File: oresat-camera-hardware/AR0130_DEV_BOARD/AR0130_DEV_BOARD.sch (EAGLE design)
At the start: 60 parts, among them J2 4-1734592-0, U10 SN74AVCB164245VR, U11 KC2520B27.0000C10E00, U12 TPS71818-33DRVT, U13 SN74AVCH8T245RHLR, U14 TPS71928-28DRVT, U15 TPS71928-28DRVT, U6 MCP9808T-E/MCDFN8_2X3MC-M, U7 MCP9808T-E/MCDFN8_2X3MC-M, U9 TCA9509DGKRDGK8-M

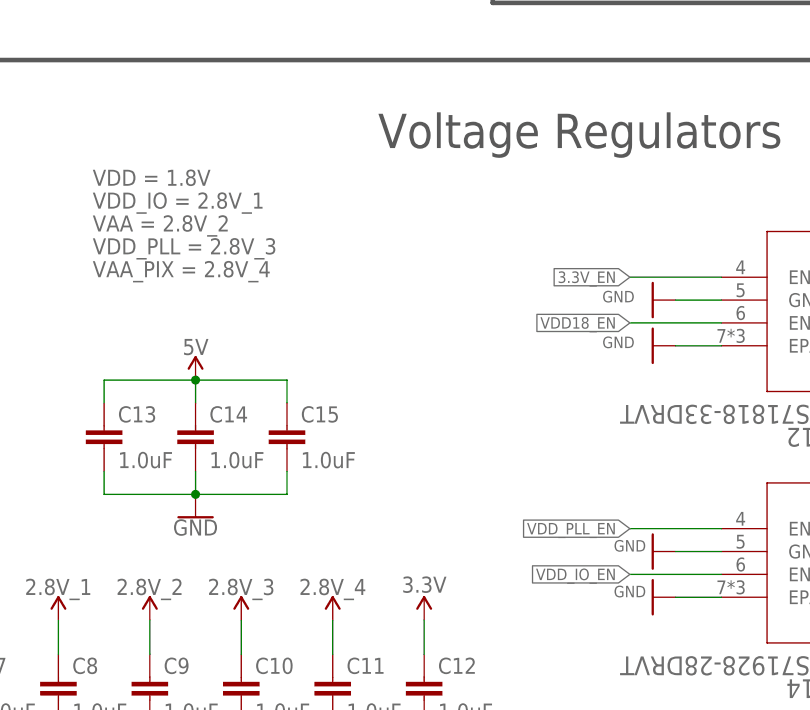
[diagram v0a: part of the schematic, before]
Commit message: added a LED
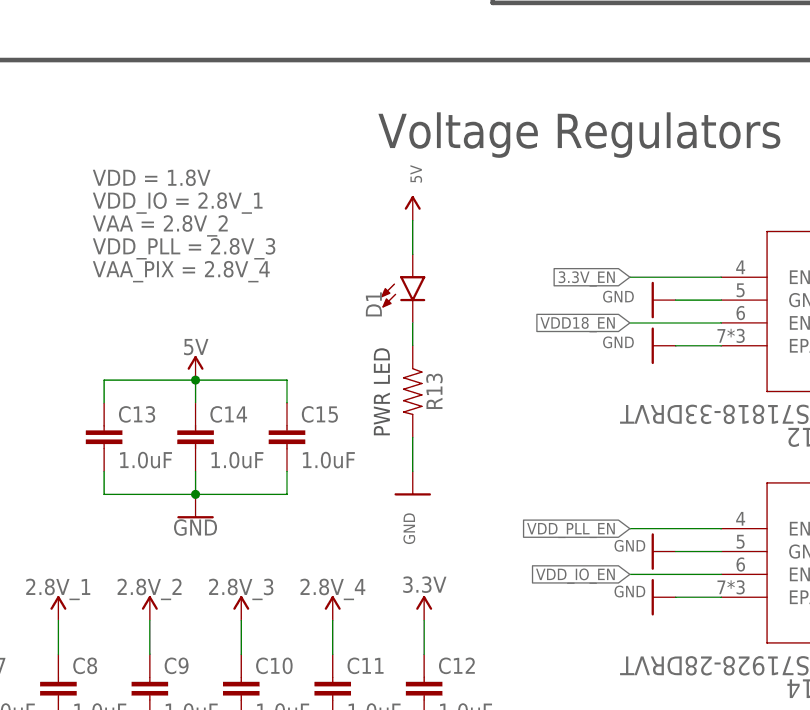
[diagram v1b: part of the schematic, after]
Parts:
- added D1: (no value), SparkFun-LED:LED0603
- added R13: (no value), SparkFun-Resistors:RESISTOR0402
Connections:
- new net N$2: D1.C, R13.1
- net 5V: now also D1.A
- net GND: now also R13.2
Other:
- note added: "PWR LED"
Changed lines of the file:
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@@
 <setting verticaltext="up"/>
 </settings>
-<grid distance="0.05" unitdist="inch" unit="inch" style="lines" multiple="2" display="yes" altdistance="0.0125" altunitdist="inch" altunit="inch"/>
+<grid distance="0.1" unitdist="inch" unit="inch" style="lines" multiple="2" display="yes" altdistance="0.0125" altunitdist="inch" altunit="inch"/>
 <layers>
 <layer number="1" name="Top" color="4" fill="1" visible="no" active="no"/>
@@
 <part name="SUPPLY58" library="SparkFun-PowerSymbols" deviceset="2.8V" device="" value="2.8V_1"/>
 <part name="SUPPLY52" library="SparkFun-PowerSymbols" deviceset="2.8V" device="" value="2.8V_1"/>
+<part name="D1" library="SparkFun-LED" deviceset="LED" device="0603"/>
+<part name="SUPPLY56" library="SparkFun-PowerSymbols" deviceset="5V" device=""/>
+<part name="R13" library="SparkFun-Resistors" library_urn="urn:adsk.eagle:library:2058534" deviceset="RESISTOR" device="0402" package3d_urn="urn:adsk.eagle:package:2058625/2" value=" "/>
+<part name="GND44" library="SparkFun-PowerSymbols" deviceset="GND" device=""/>
 </parts>
 <sheets>
@@
 <text x="15" y="81" size="1.778" layer="97" rot="R90">IMAGE SENSOR</text>
 <text x="103" y="96" size="1.778" layer="97" rot="R270">EXTERNAL</text>
+<text x="327.66" y="101.6" size="1.778" layer="97" rot="R90">PWR LED</text>
 </plain>
 <instances>
@@
 <attribute name="VALUE" x="388.366" y="180.34" size="1.27" layer="96" rot="R90" align="bottom-center"/>
 </instance>
+<instance part="D1" gate="G$1" x="330.2" y="119.38"/>
+<instance part="SUPPLY56" gate="G$1" x="330.2" y="125.73" smashed="yes">
+<attribute name="VALUE" x="331.216" y="130.81" size="1.27" layer="96" rot="R90" align="bottom-center"/>
+</instance>
+<instance part="R13" gate="G$1" x="330.2" y="106.68" rot="R270"/>
+<instance part="GND44" gate="1" x="330.2" y="95.25" smashed="yes">
+<attribute name="VALUE" x="329.184" y="91.44" size="1.27" layer="96" rot="R90" align="top-center"/>
+</instance>
 </instances>
 <busses>
@@
 <pinref part="J2" gate="A" pin="38"/>
 <pinref part="SUPPLY50" gate="G$1" pin="5V"/>
+</segment>
+<segment>
+<pinref part="D1" gate="G$1" pin="A"/>
+<pinref part="SUPPLY56" gate="G$1" pin="5V"/>
+<wire x1="330.2" y1="121.92" x2="330.2" y2="125.73" width="0.1524" layer="91"/>
 </segment>
 </net>
@@
 <junction x="69.85" y="30.48"/>
 </segment>
+<segment>
+<pinref part="GND44" gate="1" pin="GND"/>
+<pinref part="R13" gate="G$1" pin="2"/>
+<wire x1="330.2" y1="97.79" x2="330.2" y2="101.6" width="0.1524" layer="91"/>
+</segment>
 </net>
 <net name="3.3V" class="0">
@@
 </segment>
 </net>
+<net name="N$2" class="0">
+<segment>
+<pinref part="R13" gate="G$1" pin="1"/>
+<pinref part="D1" gate="G$1" pin="C"/>
+<wire x1="330.2" y1="111.76" x2="330.2" y2="114.3" width="0.1524" layer="91"/>
+</segment>
+</net>

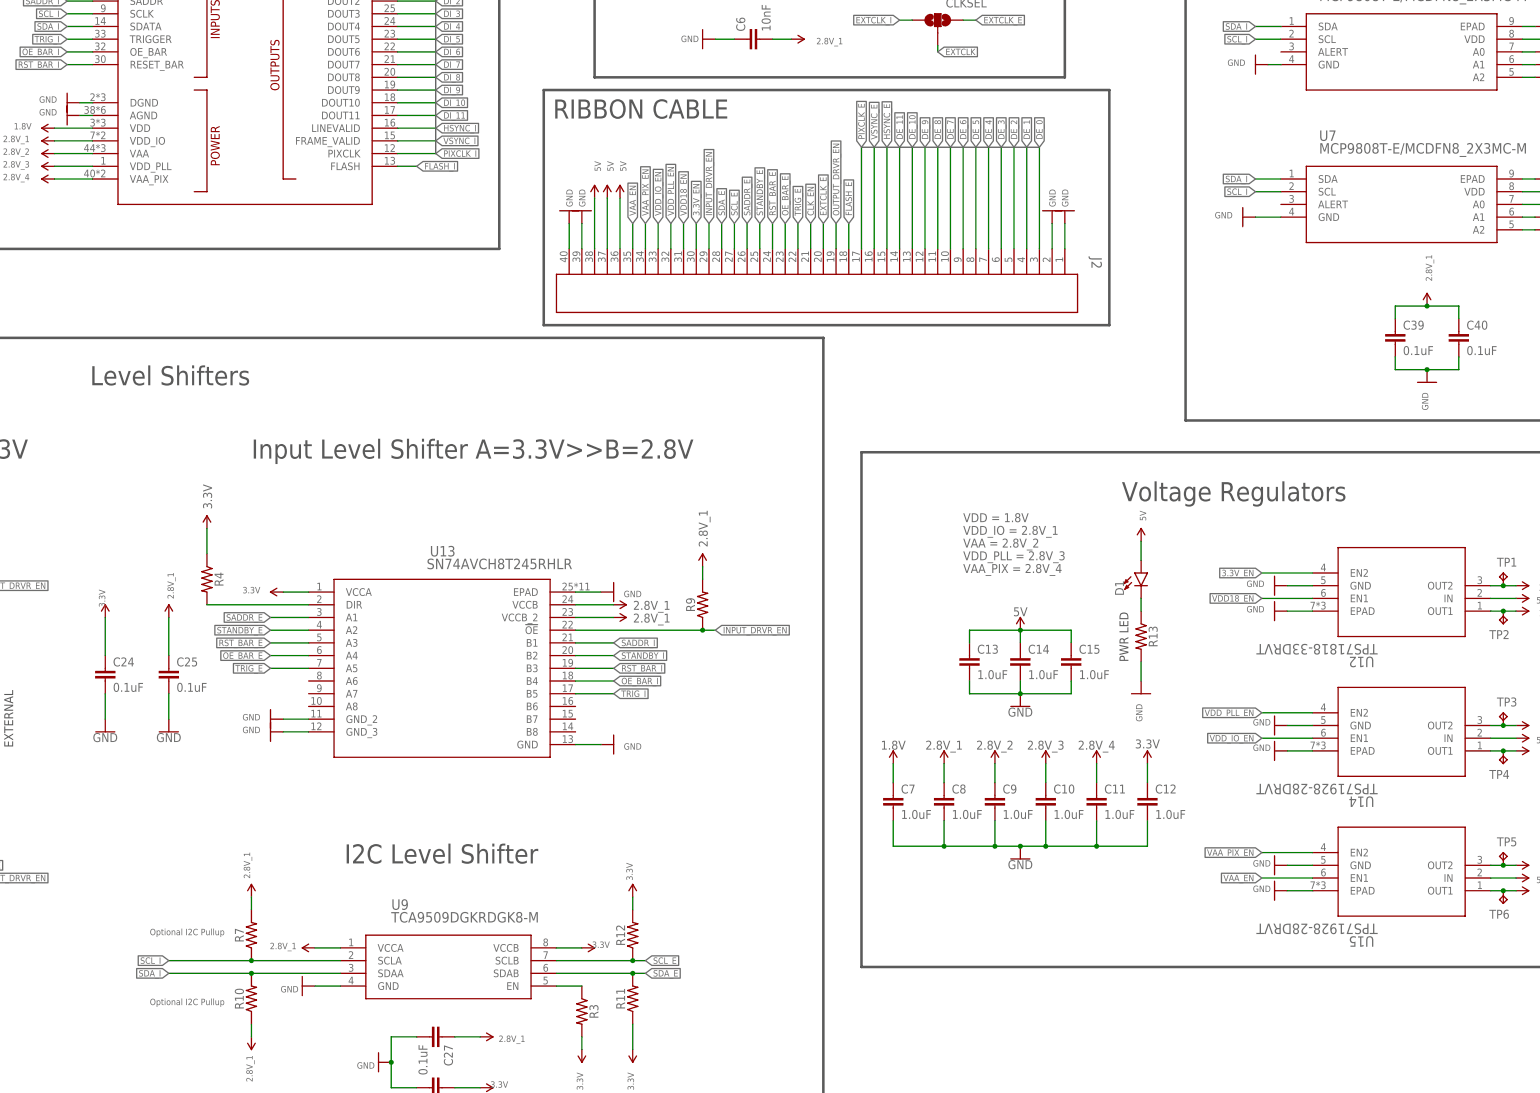
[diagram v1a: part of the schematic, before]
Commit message: cleaned up some routing, added some test points
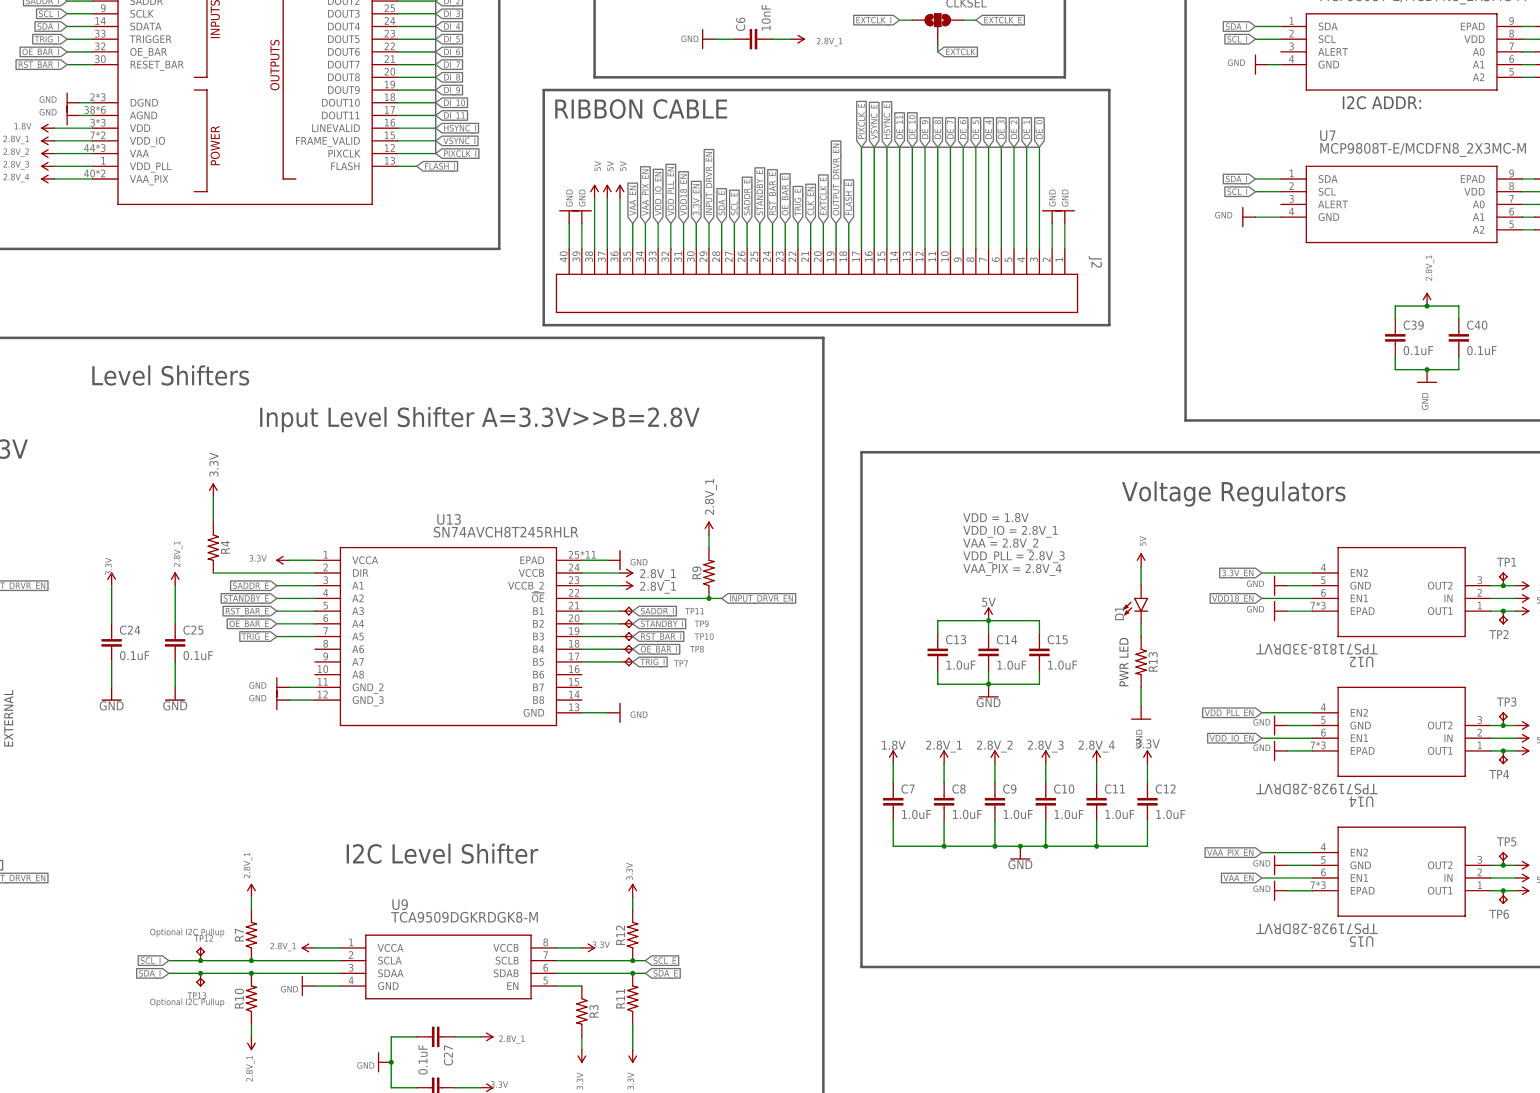
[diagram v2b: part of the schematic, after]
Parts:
- added TP10, TP11, TP12, TP13, TP7, TP8, TP9: TPTP06R, testpad:TPTP06R
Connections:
- net OE_BAR_I: now also TP8.TP
- net RST_BAR_I: now also TP9.TP
- net SADDR_I: now also TP11.TP
- net SCL_I: now also TP12.TP
- net SDA_I: now also TP13.TP
- net STANDBY_I: now also TP10.TP
- net TRIG_I: now also TP7.TP
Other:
- note added: "I2C ADDR:"
- moved on the sheet: C13, C14, C15, C24, C25, D1, R13, R4, R9, U13

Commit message: i dont know what changed, deal with it
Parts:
- C1, C2, C3, C4, C5: device Oliver_Custom:10UF-0402-16V-10% -> SparkFun-Capacitors:10UF-0603-6.3V-20%
- R1: value (none) -> 100
- R10, R11, R12, R2, R3, R4, R5, R6, R7, R8, R9: value (none) -> 10k
- R13: value (none) -> 1k
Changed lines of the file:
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@@
 <part name="U10" library="Oliver_Custom" deviceset="SN74AVCB164245VR" device=""/>
 <part name="U11" library="Oliver_Custom" deviceset="KC2520B27.0000C10E00" device=""/>
-<part name="R1" library="SparkFun-Resistors" library_urn="urn:adsk.eagle:library:2058534" deviceset="RESISTOR" device="0402" package3d_urn="urn:adsk.eagle:package:2058625/2" value=" "/>
-<part name="R2" library="SparkFun-Resistors" library_urn="urn:adsk.eagle:library:2058534" deviceset="RESISTOR" device="0402" package3d_urn="urn:adsk.eagle:package:2058625/2" value=" "/>
-<part name="R3" library="SparkFun-Resistors" library_urn="urn:adsk.eagle:library:2058534" deviceset="RESISTOR" device="0402" package3d_urn="urn:adsk.eagle:package:2058625/2" value=" "/>
+<part name="R1" library="SparkFun-Resistors" library_urn="urn:adsk.eagle:library:2058534" deviceset="RESISTOR" device="0402" package3d_urn="urn:adsk.eagle:package:2058625/2" value="100"/>
+<part name="R2" library="SparkFun-Resistors" library_urn="urn:adsk.eagle:library:2058534" deviceset="RESISTOR" device="0402" package3d_urn="urn:adsk.eagle:package:2058625/2" value="10k"/>
+<part name="R3" library="SparkFun-Resistors" library_urn="urn:adsk.eagle:library:2058534" deviceset="RESISTOR" device="0402" package3d_urn="urn:adsk.eagle:package:2058625/2" value="10k"/>
 <part name="U7" library="Oliver_Custom" deviceset="MCP9808T-E/MC" device="DFN8_2X3MC-M"/>
 <part name="U13" library="Oliver_Custom" deviceset="SN74AVCH8T245RHLR" device=""/>
-<part name="R4" library="SparkFun-Resistors" library_urn="urn:adsk.eagle:library:2058534" deviceset="RESISTOR" device="0402" package3d_urn="urn:adsk.eagle:package:2058625/2" value=" "/>
-<part name="R5" library="SparkFun-Resistors" library_urn="urn:adsk.eagle:library:2058534" deviceset="RESISTOR" device="0402" package3d_urn="urn:adsk.eagle:package:2058625/2" value=" "/>
-<part name="R6" library="SparkFun-Resistors" library_urn="urn:adsk.eagle:library:2058534" deviceset="RESISTOR" device="0402" package3d_urn="urn:adsk.eagle:package:2058625/2" value=" "/>
-<part name="R8" library="SparkFun-Resistors" library_urn="urn:adsk.eagle:library:2058534" deviceset="RESISTOR" device="0402" package3d_urn="urn:adsk.eagle:package:2058625/2" value=" "/>
-<part name="R9" library="SparkFun-Resistors" library_urn="urn:adsk.eagle:library:2058534" deviceset="RESISTOR" device="0402" package3d_urn="urn:adsk.eagle:package:2058625/2" value=" "/>
-<part name="C1" library="Oliver_Custom" library_urn="urn:adsk.eagle:library:2197211" deviceset="10UF" device="-0402-16V-10%" package3d_urn="urn:adsk.eagle:package:2054929/3" value="10uF"/>
-<part name="C2" library="Oliver_Custom" library_urn="urn:adsk.eagle:library:2197211" deviceset="10UF" device="-0402-16V-10%" package3d_urn="urn:adsk.eagle:package:2054929/3" value="10uF"/>
-<part name="C3" library="Oliver_Custom" library_urn="urn:adsk.eagle:library:2197211" deviceset="10UF" device="-0402-16V-10%" package3d_urn="urn:adsk.eagle:package:2054929/3" value="10uF"/>
-<part name="C4" library="Oliver_Custom" library_urn="urn:adsk.eagle:library:2197211" deviceset="10UF" device="-0402-16V-10%" package3d_urn="urn:adsk.eagle:package:2054929/3" value="10uF"/>
-<part name="C5" library="Oliver_Custom" library_urn="urn:adsk.eagle:library:2197211" deviceset="10UF" device="-0402-16V-10%" package3d_urn="urn:adsk.eagle:package:2054929/3" value="10uF"/>
+<part name="R4" library="SparkFun-Resistors" library_urn="urn:adsk.eagle:library:2058534" deviceset="RESISTOR" device="0402" package3d_urn="urn:adsk.eagle:package:2058625/2" value="10k"/>
+<part name="R5" library="SparkFun-Resistors" library_urn="urn:adsk.eagle:library:2058534" deviceset="RESISTOR" device="0402" package3d_urn="urn:adsk.eagle:package:2058625/2" value="10k"/>
+<part name="R6" library="SparkFun-Resistors" library_urn="urn:adsk.eagle:library:2058534" deviceset="RESISTOR" device="0402" package3d_urn="urn:adsk.eagle:package:2058625/2" value="10k"/>
+<part name="R8" library="SparkFun-Resistors" library_urn="urn:adsk.eagle:library:2058534" deviceset="RESISTOR" device="0402" package3d_urn="urn:adsk.eagle:package:2058625/2" value="10k"/>
+<part name="R9" library="SparkFun-Resistors" library_urn="urn:adsk.eagle:library:2058534" deviceset="RESISTOR" device="0402" package3d_urn="urn:adsk.eagle:package:2058625/2" value="10k"/>
+<part name="C1" library="SparkFun-Capacitors" deviceset="10UF" device="-0603-6.3V-20%" value="10uF"/>
+<part name="C2" library="SparkFun-Capacitors" deviceset="10UF" device="-0603-6.3V-20%" value="10uF"/>
+<part name="C3" library="SparkFun-Capacitors" deviceset="10UF" device="-0603-6.3V-20%" value="10uF"/>
+<part name="C4" library="SparkFun-Capacitors" deviceset="10UF" device="-0603-6.3V-20%" value="10uF"/>
+<part name="C5" library="SparkFun-Capacitors" deviceset="10UF" device="-0603-6.3V-20%" value="10uF"/>
 <part name="C13" library="SparkFun-Capacitors" deviceset="1.0UF" device="-0402-16V-10%" value="1.0uF"/>
 <part name="C14" library="SparkFun-Capacitors" deviceset="1.0UF" device="-0402-16V-10%" value="1.0uF"/>
@@
 <part name="U14" library="Oliver_Custom" deviceset="TPS71928-28DRVT" device=""/>
 <part name="U15" library="Oliver_Custom" deviceset="TPS71928-28DRVT" device=""/>
-<part name="R7" library="SparkFun-Resistors" library_urn="urn:adsk.eagle:library:2058534" deviceset="RESISTOR" device="0402" package3d_urn="urn:adsk.eagle:package:2058625/2" value=" "/>
-<part name="R10" library="SparkFun-Resistors" library_urn="urn:adsk.eagle:library:2058534" deviceset="RESISTOR" device="0402" package3d_urn="urn:adsk.eagle:package:2058625/2" value=" "/>
-<part name="R11" library="SparkFun-Resistors" library_urn="urn:adsk.eagle:library:2058534" deviceset="RESISTOR" device="0402" package3d_urn="urn:adsk.eagle:package:2058625/2" value=" "/>
-<part name="R12" library="SparkFun-Resistors" library_urn="urn:adsk.eagle:library:2058534" deviceset="RESISTOR" device="0402" package3d_urn="urn:adsk.eagle:package:2058625/2" value=" "/>
+<part name="R7" library="SparkFun-Resistors" library_urn="urn:adsk.eagle:library:2058534" deviceset="RESISTOR" device="0402" package3d_urn="urn:adsk.eagle:package:2058625/2" value="10k"/>
+<part name="R10" library="SparkFun-Resistors" library_urn="urn:adsk.eagle:library:2058534" deviceset="RESISTOR" device="0402" package3d_urn="urn:adsk.eagle:package:2058625/2" value="10k"/>
+<part name="R11" library="SparkFun-Resistors" library_urn="urn:adsk.eagle:library:2058534" deviceset="RESISTOR" device="0402" package3d_urn="urn:adsk.eagle:package:2058625/2" value="10k"/>
+<part name="R12" library="SparkFun-Resistors" library_urn="urn:adsk.eagle:library:2058534" deviceset="RESISTOR" device="0402" package3d_urn="urn:adsk.eagle:package:2058625/2" value="10k"/>
 <part name="JP1" library="SparkFun-Passives" deviceset="SOLDERJUMPER_2WAY" device="PASTE1&amp;2" value="CLKSEL"/>
 <part name="GND1" library="SparkFun-PowerSymbols" deviceset="GND" device=""/>
@@
 <part name="D1" library="SparkFun-LED" deviceset="LED" device="0603"/>
 <part name="SUPPLY56" library="SparkFun-PowerSymbols" deviceset="5V" device=""/>
-<part name="R13" library="SparkFun-Resistors" library_urn="urn:adsk.eagle:library:2058534" deviceset="RESISTOR" device="0402" package3d_urn="urn:adsk.eagle:package:2058625/2" value=" "/>
+<part name="R13" library="SparkFun-Resistors" library_urn="urn:adsk.eagle:library:2058534" deviceset="RESISTOR" device="0402" package3d_urn="urn:adsk.eagle:package:2058625/2" value="1k"/>
 <part name="GND44" library="SparkFun-PowerSymbols" deviceset="GND" device=""/>
 <part name="TP7" library="testpad" deviceset="TP" device="TP06R" package3d_urn="urn:adsk.eagle:package:27954/1"/>
@@
 <text x="15" y="81" size="1.778" layer="97" rot="R90">IMAGE SENSOR</text>
 <text x="103" y="96" size="1.778" layer="97" rot="R270">EXTERNAL</text>
-<text x="327.66" y="96.52" size="1.778" layer="97" rot="R90">PWR LED</text>
+<text x="325.12" y="96.52" size="1.778" layer="97" rot="R90">PWR LED</text>
 <text x="370.205" y="212.09" size="2.54" layer="97">I2C ADDR: </text>
 </plain>

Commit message: final board revisions
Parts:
- U$2: value AR0130CSSM00SPCA0−DRBR1-847AC -> AR0130CSSM00SPCA0−DRBR1-847AB; device Oliver_Custom:AR0130CSSM00SPCA0−DRBR1-847AC -> Oliver_Custom:AR0130CSSM00SPCA0−DRBR1-847AB
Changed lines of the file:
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@@
 <part name="SUPPLY2" library="SparkFun-PowerSymbols" deviceset="2.8V" device="" value="2.8V_1"/>
 <part name="SUPPLY3" library="SparkFun-PowerSymbols" deviceset="3.3V" device=""/>
-<part name="U$2" library="Oliver_Custom" deviceset="AR0130CSSM00SPCA0−DRBR1-847AC" device=""/>
+<part name="U$2" library="Oliver_Custom" deviceset="AR0130CSSM00SPCA0−DRBR1-847AB" device=""/>
 <part name="GND3" library="SparkFun-PowerSymbols" deviceset="GND" device=""/>
 <part name="GND4" library="SparkFun-PowerSymbols" deviceset="GND" device=""/>
